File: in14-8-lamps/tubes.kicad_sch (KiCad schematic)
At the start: 20 parts

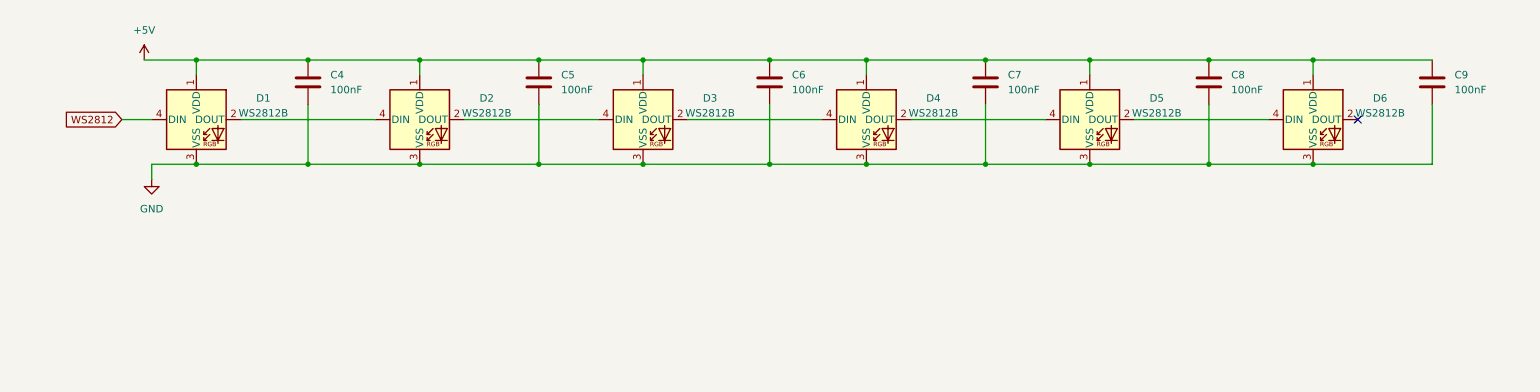
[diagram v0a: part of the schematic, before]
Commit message: add button and ws2812 connector
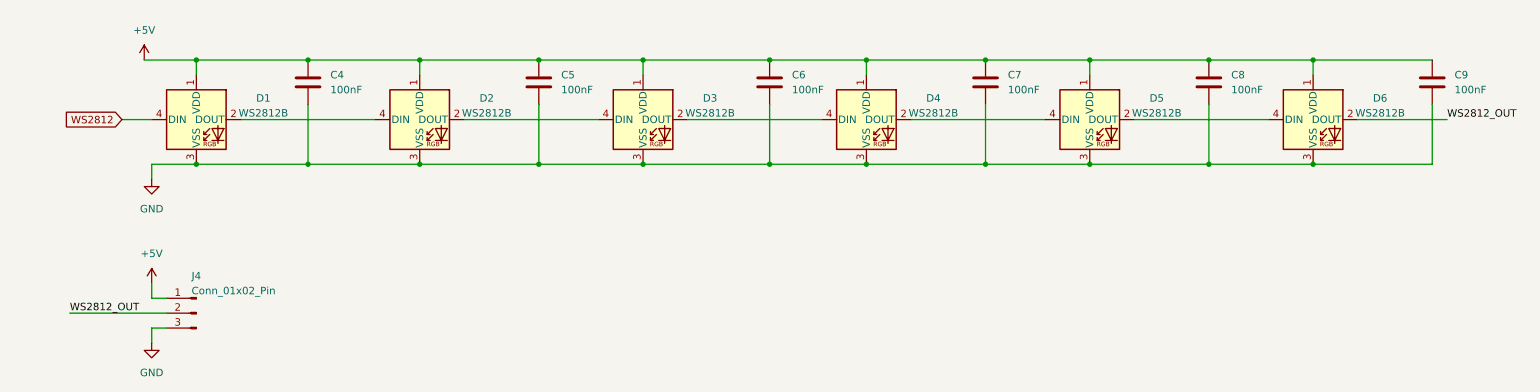
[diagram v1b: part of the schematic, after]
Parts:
- added J4: Conn_01x02_Pin, Connector_PinHeader_2.54mm:PinHeader_1x03_P2.54mm_Vertical, symbol Connector:Conn_01x03_Pin
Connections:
- net +5V: now also J4.1 (Pin_1)
- net GND: now also J4.3 (Pin_3)
- net WS2812_OUT: now reaches D6.2 (DOUT)
- net WS2812_OUT: now also J4.2 (Pin_2)
- no-connect marks 13 -> 12
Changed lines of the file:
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@@
   (no_connect (at 45.72 85.09))
   (no_connect (at 248.92 57.15))
-  (no_connect (at 248.92 139.7))
   (no_connect (at 147.32 34.29))
   (no_connect (at 248.92 34.29))
@@
     (stroke (width 0) (type default))
   )
+  (wire (pts (xy 43.18 170.18) (xy 43.18 167.64))
+    (stroke (width 0) (type default))
+  )
   (wire (pts (xy 76.2 81.28) (xy 76.2 83.82))
     (stroke (width 0) (type default))
@@
     (stroke (width 0) (type default))
   )
+  (wire (pts (xy 43.18 175.26) (xy 45.72 175.26))
+    (stroke (width 0) (type default))
+  )
   (wire (pts (xy 27.94 95.25) (xy 30.48 95.25))
     (stroke (width 0) (type default))
@@
     (stroke (width 0) (type default))
   )
+  (wire (pts (xy 248.92 139.7) (xy 264.16 139.7))
+    (stroke (width 0) (type default))
+  )
   (wire (pts (xy 27.94 39.37) (xy 30.48 39.37))
     (stroke (width 0) (type default))
@@
     (stroke (width 0) (type default))
   )
+  (wire (pts (xy 45.72 170.18) (xy 43.18 170.18))
+    (stroke (width 0) (type default))
+  )
   (wire (pts (xy 78.74 57.15) (xy 81.28 57.15))
     (stroke (width 0) (type default))
@@
     (stroke (width 0) (type default))
   )
+  (wire (pts (xy 43.18 177.8) (xy 43.18 175.26))
+    (stroke (width 0) (type default))
+  )
   (wire (pts (xy 41.91 129.54) (xy 50.8 129.54))
     (stroke (width 0) (type default))
@@
     (stroke (width 0) (type default))
   )
+  (wire (pts (xy 29.21 172.72) (xy 45.72 172.72))
+    (stroke (width 0) (type default))
+  )
   (wire (pts (xy 203.2 129.54) (xy 203.2 132.08))
     (stroke (width 0) (type default))
@@
   (wire (pts (xy 45.72 44.45) (xy 48.26 44.45))
     (stroke (width 0) (type default))
+  )
+  (label "WS2812_OUT" (at 29.21 172.72 0) (fields_autoplaced)
+    (effects (font (size 1.27 1.27)) (justify left bottom))
+  )
+  (label "WS2812_OUT" (at 264.16 139.7 0) (fields_autoplaced)
+    (effects (font (size 1.27 1.27)) (justify left bottom))
   )
   (global_label "DIG6" (shape input) (at 129.54 49.53 180) (fields_autoplaced)
@@
     (property "Intersheetrefs" "${INTERSHEET_REFS}" (at 20.6005 102.87 0)
       (effects (font (size 1.27 1.27)) (justify right) hide)
+    )
+  )
+  (symbol (lib_id "power:GND") (at 43.18 177.8 0) (unit 1)
+    (in_bom yes) (on_board yes) (dnp no) (fields_autoplaced)
+    (property "Reference" "#PWR029" (at 43.18 184.15 0)
+      (effects (font (size 1.27 1.27)) hide)
+    )
+    (property "Value" "GND" (at 43.18 182.88 0)
+      (effects (font (size 1.27 1.27)))
+    )
+    (property "Footprint" "" (at 43.18 177.8 0)
+      (effects (font (size 1.27 1.27)) hide)
+    )
+    (property "Datasheet" "" (at 43.18 177.8 0)
+      (effects (font (size 1.27 1.27)) hide)
+    )
+    (pin "1")
+    (instances
+      (project "nixie-clock-esp-32"
+        (path "/cd8918ee-e986-4b1b-bef5-f32ed2eef1b1/06f34b52-5a6a-4de1-84d0-e5bfe04d78e4"
+          (reference "#PWR029") (unit 1)
+        )
+      )
     )
   )
@@
         )
       )
+    )
+  )
+  (symbol (lib_id "Connector:Conn_01x03_Pin") (at 50.8 172.72 0) (mirror y) (unit 1)
+    (in_bom yes) (on_board yes) (dnp no)
+    (property "Reference" "J4" (at 50.8 166.37 0)
+      (effects (font (size 1.27 1.27)))
+    )
+    (property "Value" "Conn_01x02_Pin" (at 57.15 168.91 0)
+      (effects (font (size 1.27 1.27)))
+    )
+    (property "Footprint" "Connector_PinHeader_2.54mm:PinHeader_1x03_P2.54mm_Vertical" (at 50.8 172.72 0)
+      (effects (font (size 1.27 1.27)) hide)
+    )
+    (property "Datasheet" "~" (at 50.8 172.72 0)
+      (effects (font (size 1.27 1.27)) hide)
+    )
+    (pin "1")
+    (pin "2")
+    (pin "3")
+    (instances
+      (project "nixie-clock-esp-32"
+        (path "/cd8918ee-e986-4b1b-bef5-f32ed2eef1b1/06f34b52-5a6a-4de1-84d0-e5bfe04d78e4"
+          (reference "J4") (unit 1)
+        )
+      )
+    )
+  )
+  (symbol (lib_id "power:+5V") (at 43.18 167.64 0) (unit 1)
+    (in_bom yes) (on_board yes) (dnp no) (fields_autoplaced)
+    (property "Reference" "#PWR028" (at 43.18 171.45 0)
+      (effects (font (size 1.27 1.27)) hide)
+    )
+    (property "Value" "+5V" (at 43.18 162.56 0)
+      (effects (font (size 1.27 1.27)))
+    )
+    (property "Footprint" "" (at 43.18 167.64 0)
+      (effects (font (size 1.27 1.27)) hide)
+    )
+    (property "Datasheet" "" (at 43.18 167.64 0)
+      (effects (font (size 1.27 1.27)) hide)
+    )
+    (pin "1")
+    (instances
+      (project "nixie-clock-esp-32"
+        (path "/cd8918ee-e986-4b1b-bef5-f32ed2eef1b1/06f34b52-5a6a-4de1-84d0-e5bfe04d78e4"
+          (reference "#PWR028") (unit 1)
+        )
+      )
